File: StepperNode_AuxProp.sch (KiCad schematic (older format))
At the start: 7 parts, among them P10 TE_640456-8, P11 TE_640456-8, U19 MAX4948ETG+, U20 NUD3124LT1G

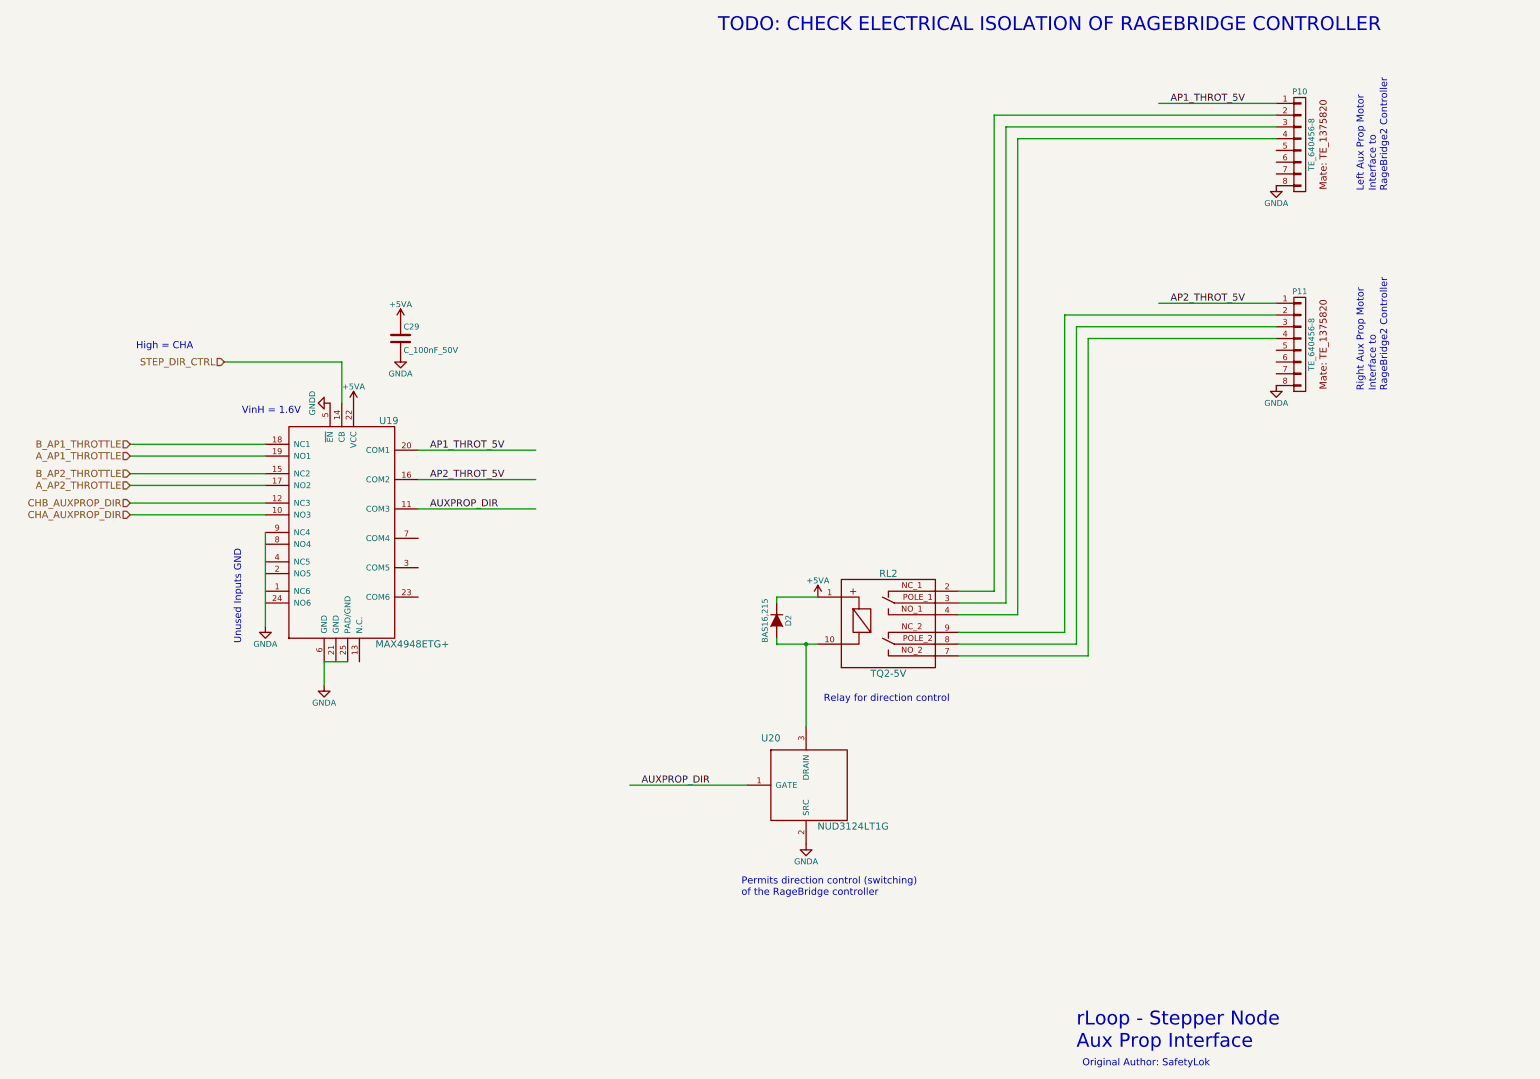
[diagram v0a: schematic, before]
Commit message: Fix most ERC warnings (non-connected pins, etc)
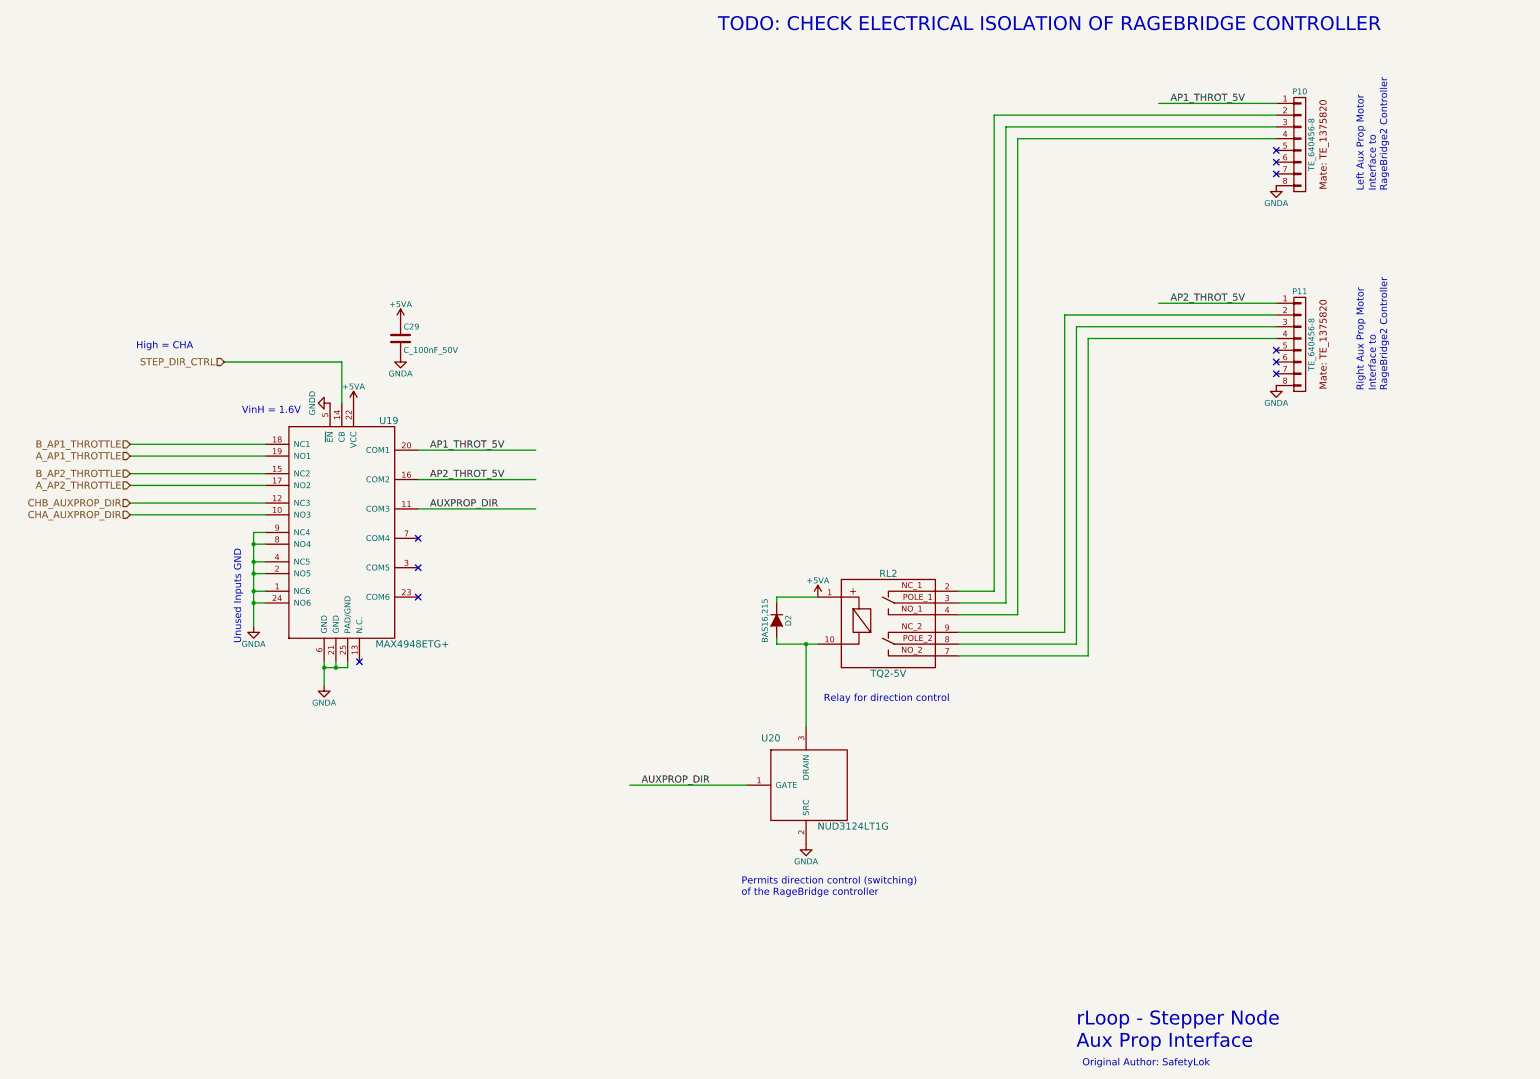
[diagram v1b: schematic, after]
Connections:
- wire segments 40 -> 48
- no-connect marks 0 -> 10
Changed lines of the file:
@@
 CHB_AUXPROP_DIR
 $Comp
-L +5VA #PWR122
+L +5VA #PWR0129
 U 1 1 5756511D
 P 5750 4850
-F 0 "#PWR122" H 5750 4700 50  0001 C CNN
+F 0 "#PWR0129" H 5750 4700 50  0001 C CNN
 F 1 "+5VA" H 5750 4990 50  0000 C CNN
 F 2 "" H 5750 4850 50  0000 C CNN
@@
 $EndComp
 $Comp
-L +5VA #PWR123
+L +5VA #PWR0130
 U 1 1 575651A0
 P 6150 4150
-F 0 "#PWR123" H 6150 4000 50  0001 C CNN
+F 0 "#PWR0130" H 6150 4000 50  0001 C CNN
 F 1 "+5VA" H 6150 4290 50  0000 C CNN
 F 2 "" H 6150 4150 50  0000 C CNN
@@
 $EndComp
 $Comp
-L GNDA #PWR119
+L GNDA #PWR0131
 U 1 1 575651AF
-P 5000 6750
-F 0 "#PWR119" H 5000 6500 50  0001 C CNN
-F 1 "GNDA" H 5000 6600 50  0000 C CNN
-F 2 "" H 5000 6750 50  0000 C CNN
-F 3 "" H 5000 6750 50  0000 C CNN
-	1    5000 6750
+P 4900 6750
+F 0 "#PWR0131" H 4900 6500 50  0001 C CNN
+F 1 "GNDA" H 4900 6600 50  0000 C CNN
+F 2 "" H 4900 6750 50  0000 C CNN
+F 3 "" H 4900 6750 50  0000 C CNN
+	1    4900 6750
 	1    0    0    -1
 $EndComp
@@
 VinH = 1.6V
 $Comp
-L GNDD #PWR121
+L GNDD #PWR0132
 U 1 1 57565359
 P 5550 4850
-F 0 "#PWR121" H 5550 4600 50  0001 C CNN
+F 0 "#PWR0132" H 5550 4600 50  0001 C CNN
 F 1 "GNDD" H 5550 4700 50  0000 C CNN
 F 2 "" H 5550 4850 50  0000 C CNN
@@
 	5000 5550 3850 5550
 Wire Wire Line
-	5700 7050 5500 7050
-Wire Wire Line
 	5500 7050 5500 7250
 Text Notes 4800 6900 1    60   ~ 0
 Unused Inputs GND
 $Comp
-L GNDA #PWR124
+L GNDA #PWR0133
 U 1 1 5756652B
 P 6150 4450
-F 0 "#PWR124" H 6150 4200 50  0001 C CNN
+F 0 "#PWR0133" H 6150 4200 50  0001 C CNN
 F 1 "GNDA" H 6150 4300 50  0000 C CNN
 F 2 "" H 6150 4450 50  0000 C CNN
@@
 $EndComp
 $Comp
-L GNDA #PWR120
+L GNDA #PWR0134
 U 1 1 5756673C
 P 5500 7250
-F 0 "#PWR120" H 5500 7000 50  0001 C CNN
+F 0 "#PWR0134" H 5500 7000 50  0001 C CNN
 F 1 "GNDA" H 5500 7100 50  0000 C CNN
 F 2 "" H 5500 7250 50  0000 C CNN
@@
 AP2_THROT_5V
 Wire Wire Line
-	5000 5950 5000 6750
-Wire Wire Line
 	5000 5700 3850 5700
 Wire Wire Line
@@
 AUXPROP_DIR
 $Comp
-L +5VA #PWR126
+L +5VA #PWR0135
 U 1 1 575C0D8C
 P 9700 6500
-F 0 "#PWR126" H 9700 6350 50  0001 C CNN
+F 0 "#PWR0135" H 9700 6350 50  0001 C CNN
 F 1 "+5VA" H 9700 6640 50  0000 C CNN
 F 2 "" H 9700 6500 50  0000 C CNN
@@
 	9350 6500 9350 6550
 Wire Wire Line
-	9700 6900 9350 6900
+	9350 6900 9700 6900
 Wire Wire Line
 	9350 6900 9350 6850
@@
 Connection ~ 9600 6900
 $Comp
-L GNDA #PWR125
+L GNDA #PWR0136
 U 1 1 575D465A
 P 9600 8600
-F 0 "#PWR125" H 9600 8350 50  0001 C CNN
+F 0 "#PWR0136" H 9600 8350 50  0001 C CNN
 F 1 "GNDA" H 9600 8450 50  0000 C CNN
 F 2 "" H 9600 8600 50  0000 C CNN
@@
 Permits direction control (switching)\nof the RageBridge controller
 $Comp
-L GNDA #PWR127
+L GNDA #PWR0137
 U 1 1 575D497D
 P 13600 3000
-F 0 "#PWR127" H 13600 2750 50  0001 C CNN
+F 0 "#PWR0137" H 13600 2750 50  0001 C CNN
 F 1 "GNDA" H 13600 2850 50  0000 C CNN
 F 2 "" H 13600 3000 50  0000 C CNN
@@
 $EndComp
 $Comp
-L GNDA #PWR128
+L GNDA #PWR0138
 U 1 1 575D498C
 P 13600 4700
-F 0 "#PWR128" H 13600 4450 50  0001 C CNN
+F 0 "#PWR0138" H 13600 4450 50  0001 C CNN
 F 1 "GNDA" H 13600 4550 50  0000 C CNN
 F 2 "" H 13600 4700 50  0000 C CNN
@@
 	1    0    0    -1
 $EndComp
+NoConn ~ 13600 2700
+NoConn ~ 13600 2800
+NoConn ~ 13600 2900
+NoConn ~ 13600 4400
+NoConn ~ 13600 4500
+NoConn ~ 13600 4600
+NoConn ~ 6300 6000
+NoConn ~ 6300 6250
+NoConn ~ 6300 6500
+Wire Wire Line
+	5000 5950 4900 5950
+Wire Wire Line
+	4900 5950 4900 6750
+Wire Wire Line
+	5000 6050 4900 6050
+Connection ~ 4900 6050
+Wire Wire Line
+	4900 6200 5000 6200
+Connection ~ 4900 6200
+Wire Wire Line
+	5000 6300 4900 6300
+Connection ~ 4900 6300
+Wire Wire Line
+	4900 6450 5000 6450
+Connection ~ 4900 6450
+Wire Wire Line
+	5000 6550 4900 6550
+Connection ~ 4900 6550
+NoConn ~ 5800 7050
+Wire Wire Line
+	5600 7050 5600 7100
+Wire Wire Line
+	5500 7100 5700 7100
+Connection ~ 5500 7100
+Wire Wire Line
+	5700 7100 5700 7050
+Connection ~ 5600 7100
 $EndSCHEMATC

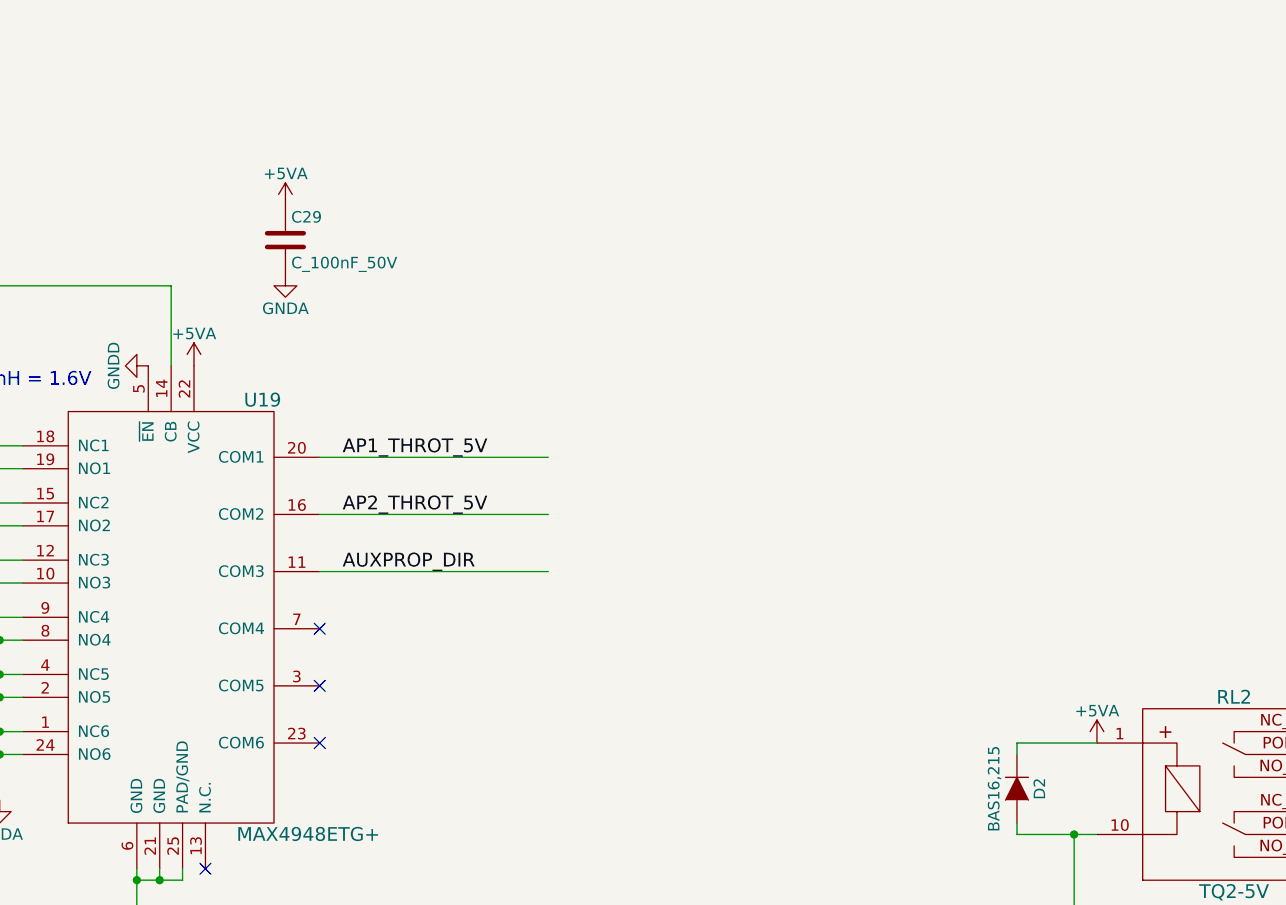
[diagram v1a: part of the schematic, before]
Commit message: Finish isolation and add brake limit switches.
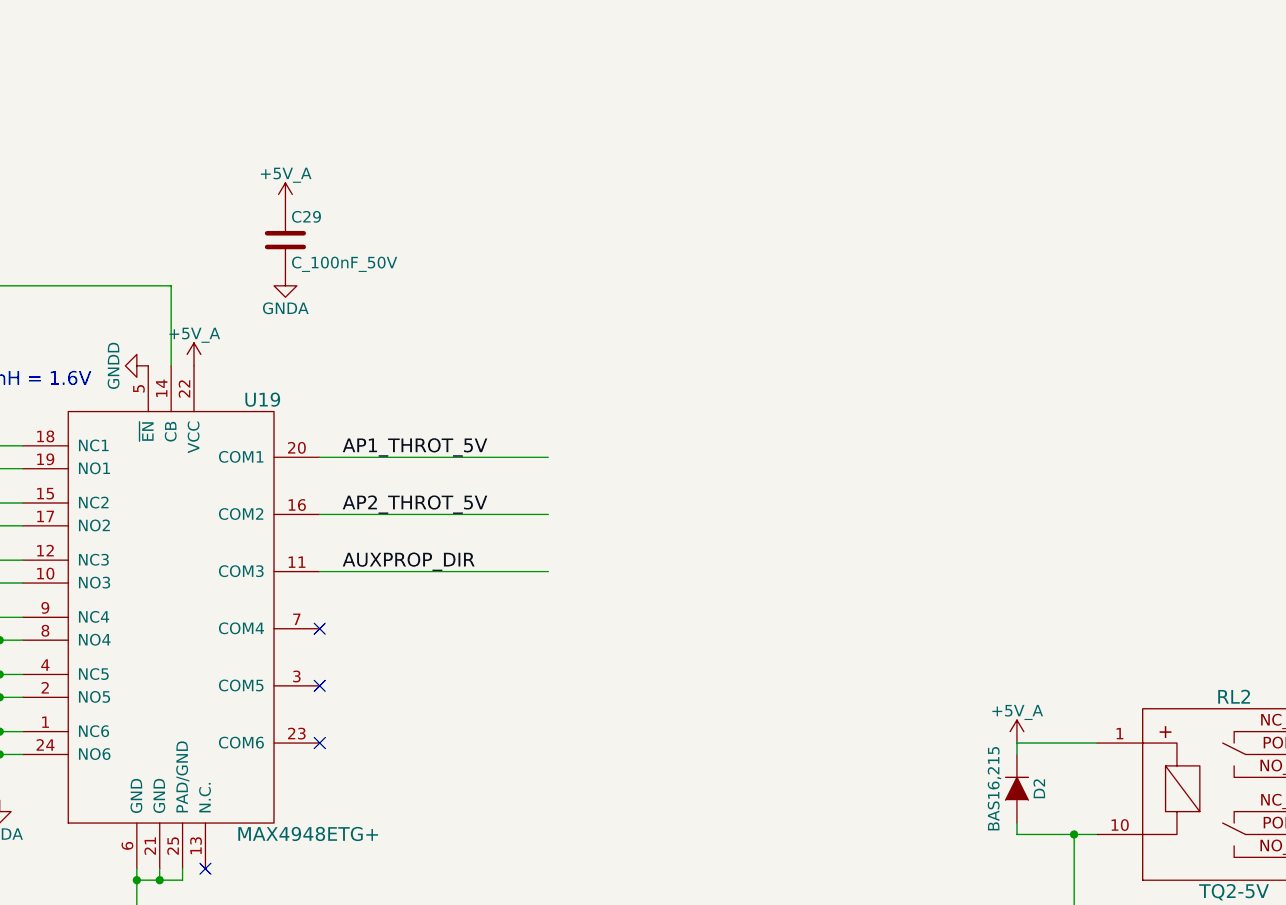
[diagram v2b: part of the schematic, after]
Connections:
- net labels added: +5V_A
- net labels removed: +5VA
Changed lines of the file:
@@
 CHB_AUXPROP_DIR
 $Comp
-L +5VA #PWR0129
-U 1 1 5756511D
-P 5750 4850
-F 0 "#PWR0129" H 5750 4700 50  0001 C CNN
-F 1 "+5VA" H 5750 4990 50  0000 C CNN
-F 2 "" H 5750 4850 50  0000 C CNN
-F 3 "" H 5750 4850 50  0000 C CNN
-	1    5750 4850
-	1    0    0    -1
-$EndComp
-$Comp
-L +5VA #PWR0130
-U 1 1 575651A0
-P 6150 4150
-F 0 "#PWR0130" H 6150 4000 50  0001 C CNN
-F 1 "+5VA" H 6150 4290 50  0000 C CNN
-F 2 "" H 6150 4150 50  0000 C CNN
-F 3 "" H 6150 4150 50  0000 C CNN
-	1    6150 4150
-	1    0    0    -1
-$EndComp
-$Comp
-L GNDA #PWR0131
+L GNDA #PWR168
 U 1 1 575651AF
 P 4900 6750
-F 0 "#PWR0131" H 4900 6500 50  0001 C CNN
+F 0 "#PWR168" H 4900 6500 50  0001 C CNN
 F 1 "GNDA" H 4900 6600 50  0000 C CNN
 F 2 "" H 4900 6750 50  0000 C CNN
@@
 VinH = 1.6V
 $Comp
-L GNDD #PWR0132
+L GNDD #PWR170
 U 1 1 57565359
 P 5550 4850
-F 0 "#PWR0132" H 5550 4600 50  0001 C CNN
+F 0 "#PWR170" H 5550 4600 50  0001 C CNN
 F 1 "GNDD" H 5550 4700 50  0000 C CNN
 F 2 "" H 5550 4850 50  0000 C CNN
@@
 Unused Inputs GND
 $Comp
-L GNDA #PWR0133
+L GNDA #PWR173
 U 1 1 5756652B
 P 6150 4450
-F 0 "#PWR0133" H 6150 4200 50  0001 C CNN
+F 0 "#PWR173" H 6150 4200 50  0001 C CNN
 F 1 "GNDA" H 6150 4300 50  0000 C CNN
 F 2 "" H 6150 4450 50  0000 C CNN
@@
 $EndComp
 $Comp
-L GNDA #PWR0134
+L GNDA #PWR169
 U 1 1 5756673C
 P 5500 7250
-F 0 "#PWR0134" H 5500 7000 50  0001 C CNN
+F 0 "#PWR169" H 5500 7000 50  0001 C CNN
 F 1 "GNDA" H 5500 7100 50  0000 C CNN
 F 2 "" H 5500 7250 50  0000 C CNN
@@
 Text Label 6400 5750 0    60   ~ 0
 AUXPROP_DIR
-$Comp
-L +5VA #PWR0135
-U 1 1 575C0D8C
-P 9700 6500
-F 0 "#PWR0135" H 9700 6350 50  0001 C CNN
-F 1 "+5VA" H 9700 6640 50  0000 C CNN
-F 2 "" H 9700 6500 50  0000 C CNN
-F 3 "" H 9700 6500 50  0000 C CNN
-	1    9700 6500
-	1    0    0    -1
-$EndComp
 Wire Wire Line
 	8100 8100 9100 8100
@@
 Connection ~ 9600 6900
 $Comp
-L GNDA #PWR0136
+L GNDA #PWR175
 U 1 1 575D465A
 P 9600 8600
-F 0 "#PWR0136" H 9600 8350 50  0001 C CNN
+F 0 "#PWR175" H 9600 8350 50  0001 C CNN
 F 1 "GNDA" H 9600 8450 50  0000 C CNN
 F 2 "" H 9600 8600 50  0000 C CNN
@@
 Permits direction control (switching)\nof the RageBridge controller
 $Comp
-L GNDA #PWR0137
+L GNDA #PWR176
 U 1 1 575D497D
 P 13600 3000
-F 0 "#PWR0137" H 13600 2750 50  0001 C CNN
+F 0 "#PWR176" H 13600 2750 50  0001 C CNN
 F 1 "GNDA" H 13600 2850 50  0000 C CNN
 F 2 "" H 13600 3000 50  0000 C CNN
@@
 $EndComp
 $Comp
-L GNDA #PWR0138
+L GNDA #PWR177
 U 1 1 575D498C
 P 13600 4700
-F 0 "#PWR0138" H 13600 4450 50  0001 C CNN
+F 0 "#PWR177" H 13600 4450 50  0001 C CNN
 F 1 "GNDA" H 13600 4550 50  0000 C CNN
 F 2 "" H 13600 4700 50  0000 C CNN
@@
 	5700 7100 5700 7050
 Connection ~ 5600 7100
+$Comp
+L +5V_A #PWR172
+U 1 1 57659AEC
+P 6150 4150
+F 0 "#PWR172" H 6150 4000 50  0001 C CNN
+F 1 "+5V_A" H 6150 4290 50  0000 C CNN
+F 2 "" H 6150 4150 60  0000 C CNN
+F 3 "" H 6150 4150 60  0000 C CNN
+	1    6150 4150
+	1    0    0    -1
+$EndComp
+$Comp
+L +5V_A #PWR171
+U 1 1 57659B0C
+P 5750 4850
+F 0 "#PWR171" H 5750 4700 50  0001 C CNN
+F 1 "+5V_A" H 5750 4990 50  0000 C CNN
+F 2 "" H 5750 4850 60  0000 C CNN
+F 3 "" H 5750 4850 60  0000 C CNN
+	1    5750 4850
+	1    0    0    -1
+$EndComp
+$Comp
+L +5V_A #PWR174
+U 1 1 57659D61
+P 9350 6500
+F 0 "#PWR174" H 9350 6350 50  0001 C CNN
+F 1 "+5V_A" H 9350 6640 50  0000 C CNN
+F 2 "" H 9350 6500 60  0000 C CNN
+F 3 "" H 9350 6500 60  0000 C CNN
+	1    9350 6500
+	1    0    0    -1
+$EndComp
 $EndSCHEMATC
